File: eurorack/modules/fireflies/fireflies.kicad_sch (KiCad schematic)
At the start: 37 parts, among them J1 Conn_02x05_Odd_Even, U3 ProMicro

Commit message: fireflies schematic stuff
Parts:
- added J?: (no value), symbol Connector:AudioJack2_SwitchT
- added J? (x3): AudioJack2_SwitchT, symbol Connector:AudioJack2_SwitchT
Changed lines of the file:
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@@
     (pin "2")
+  )
+  (symbol (lib_id "Connector:AudioJack2_SwitchT") (at 181.864 77.978 0) (unit 1)
+    (in_bom yes) (on_board yes) (fields_autoplaced)
+    (property "Reference" "J?" (id 0) (at 181.229 68.58 0))
+    (property "Value" "" (id 1) (at 181.229 71.12 0))
+    (property "Footprint" "" (id 2) (at 181.864 77.978 0)
+      (effects (font (size 1.27 1.27)) hide)
+    )
+    (property "Datasheet" "~" (id 3) (at 181.864 77.978 0)
+      (effects (font (size 1.27 1.27)) hide)
+    )
+    (pin "S")
+    (pin "T")
+    (pin "TN")
   )
   (symbol (lib_id "Device:R") (at 87.122 174.752 90) (unit 1)
@@
     )
     (pin "1")
+  )
+  (symbol (lib_id "Connector:AudioJack2_SwitchT") (at 180.594 100.584 0) (unit 1)
+    (in_bom yes) (on_board yes) (fields_autoplaced)
+    (property "Reference" "J?" (id 0) (at 179.959 91.186 0))
+    (property "Value" "AudioJack2_SwitchT" (id 1) (at 179.959 93.726 0))
+    (property "Footprint" "" (id 2) (at 180.594 100.584 0)
+      (effects (font (size 1.27 1.27)) hide)
+    )
+    (property "Datasheet" "~" (id 3) (at 180.594 100.584 0)
+      (effects (font (size 1.27 1.27)) hide)
+    )
+    (pin "S")
+    (pin "T")
+    (pin "TN")
   )
   (symbol (lib_id "power:GND") (at 83.312 184.912 0) (unit 1)
@@
     (pin "1")
   )
+  (symbol (lib_id "Connector:AudioJack2_SwitchT") (at 209.042 99.06 0) (unit 1)
+    (in_bom yes) (on_board yes) (fields_autoplaced)
+    (property "Reference" "J?" (id 0) (at 208.407 89.662 0))
+    (property "Value" "AudioJack2_SwitchT" (id 1) (at 208.407 92.202 0))
+    (property "Footprint" "" (id 2) (at 209.042 99.06 0)
+      (effects (font (size 1.27 1.27)) hide)
+    )
+    (property "Datasheet" "~" (id 3) (at 209.042 99.06 0)
+      (effects (font (size 1.27 1.27)) hide)
+    )
+    (pin "S")
+    (pin "T")
+    (pin "TN")
+  )
   (symbol (lib_id "power:GND") (at 41.91 145.796 0) (unit 1)
     (in_bom yes) (on_board yes) (fields_autoplaced)
@@
     )
     (pin "1")
+  )
+  (symbol (lib_id "Connector:AudioJack2_SwitchT") (at 210.566 78.232 0) (unit 1)
+    (in_bom yes) (on_board yes) (fields_autoplaced)
+    (property "Reference" "J?" (id 0) (at 209.931 68.834 0))
+    (property "Value" "AudioJack2_SwitchT" (id 1) (at 209.931 71.374 0))
+    (property "Footprint" "" (id 2) (at 210.566 78.232 0)
+      (effects (font (size 1.27 1.27)) hide)
+    )
+    (property "Datasheet" "~" (id 3) (at 210.566 78.232 0)
+      (effects (font (size 1.27 1.27)) hide)
+    )
+    (pin "S")
+    (pin "T")
+    (pin "TN")
   )
   (symbol (lib_id "power:GND") (at 52.578 133.096 270) (unit 1)
@@
       (reference "J1") (unit 1) (value "Conn_02x05_Odd_Even") (footprint "Connector_PinHeader_2.54mm:PinHeader_2x05_P2.54mm_Vertical_SMD")
     )
+    (path "/7fec32f7-4e07-4832-9024-4f9fa14f8485"
+      (reference "J?") (unit 1) (value "AudioJack2_SwitchT") (footprint "")
+    )
+    (path "/9269573e-337a-438e-bed5-4bfb6f1dd25c"
+      (reference "J?") (unit 1) (value "AudioJack2_SwitchT") (footprint "")
+    )
+    (path "/e0d100f4-64a0-4b05-af9e-33a716f9f45b"
+      (reference "J?") (unit 1) (value "AudioJack2_SwitchT") (footprint "")
+    )
+    (path "/e653be94-887e-48f2-9e69-61973902ec02"
+      (reference "J?") (unit 1) (value "AudioJack2_SwitchT") (footprint "")
+    )
     (path "/a7cbf3ab-685a-48fb-b5f0-6b3e0a12818c"

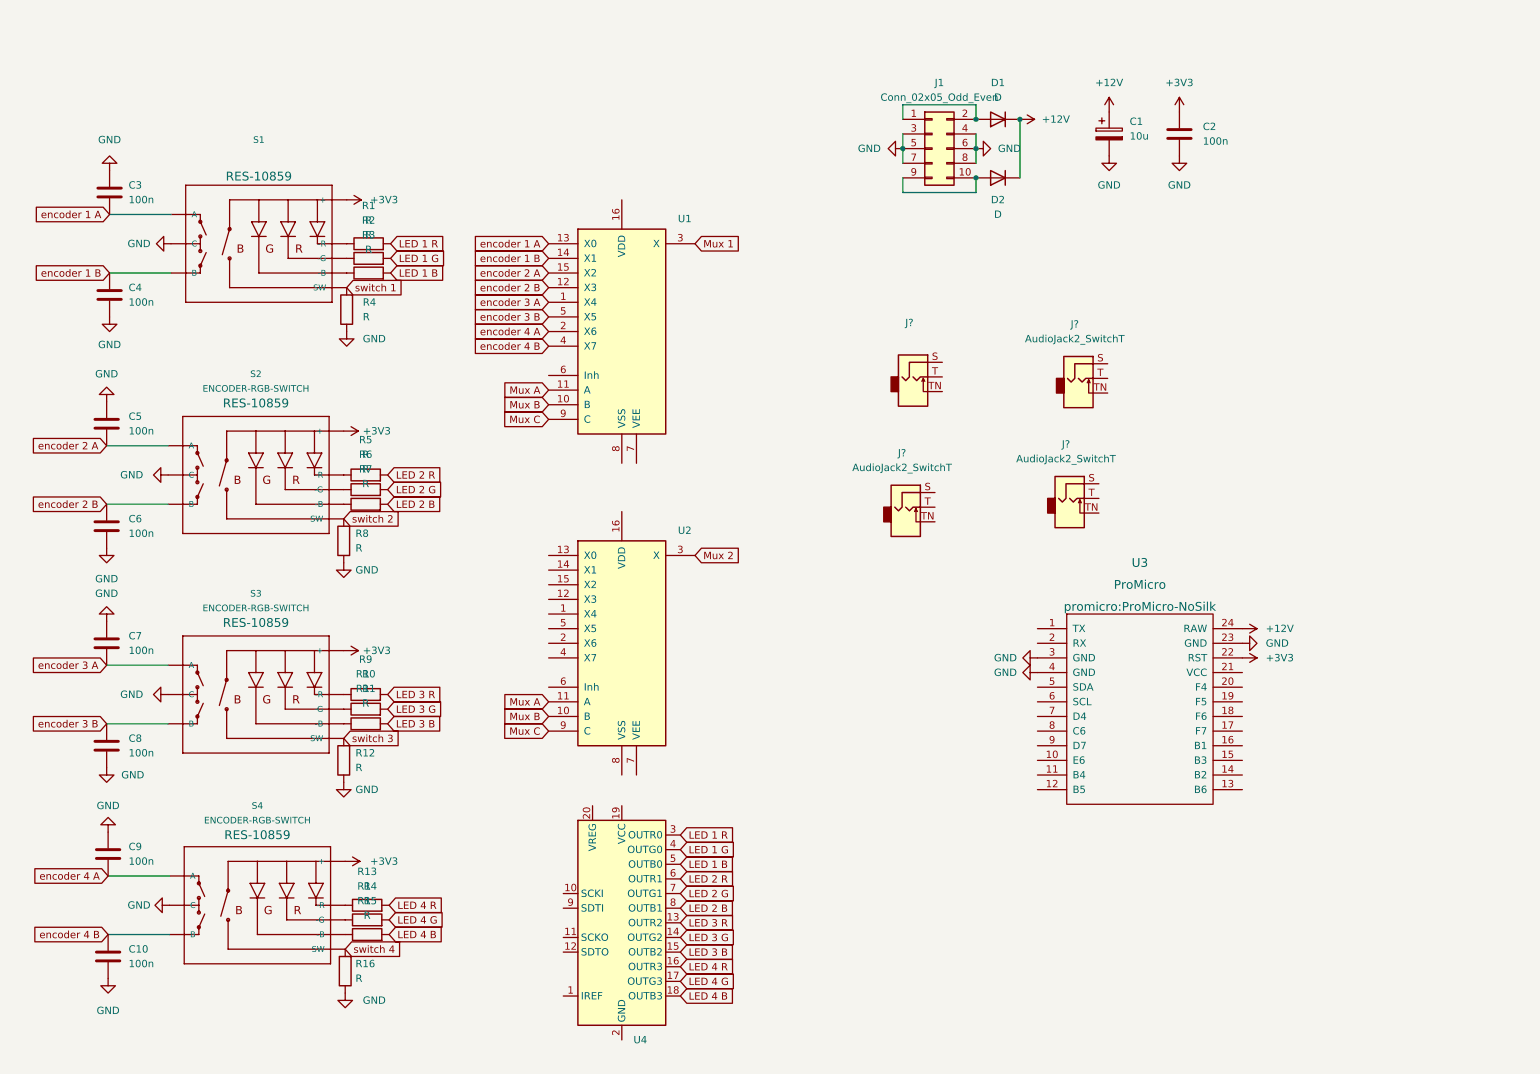
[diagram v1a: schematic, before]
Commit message: cicadas: normal clock input to 3v3 and fix missing ground connections
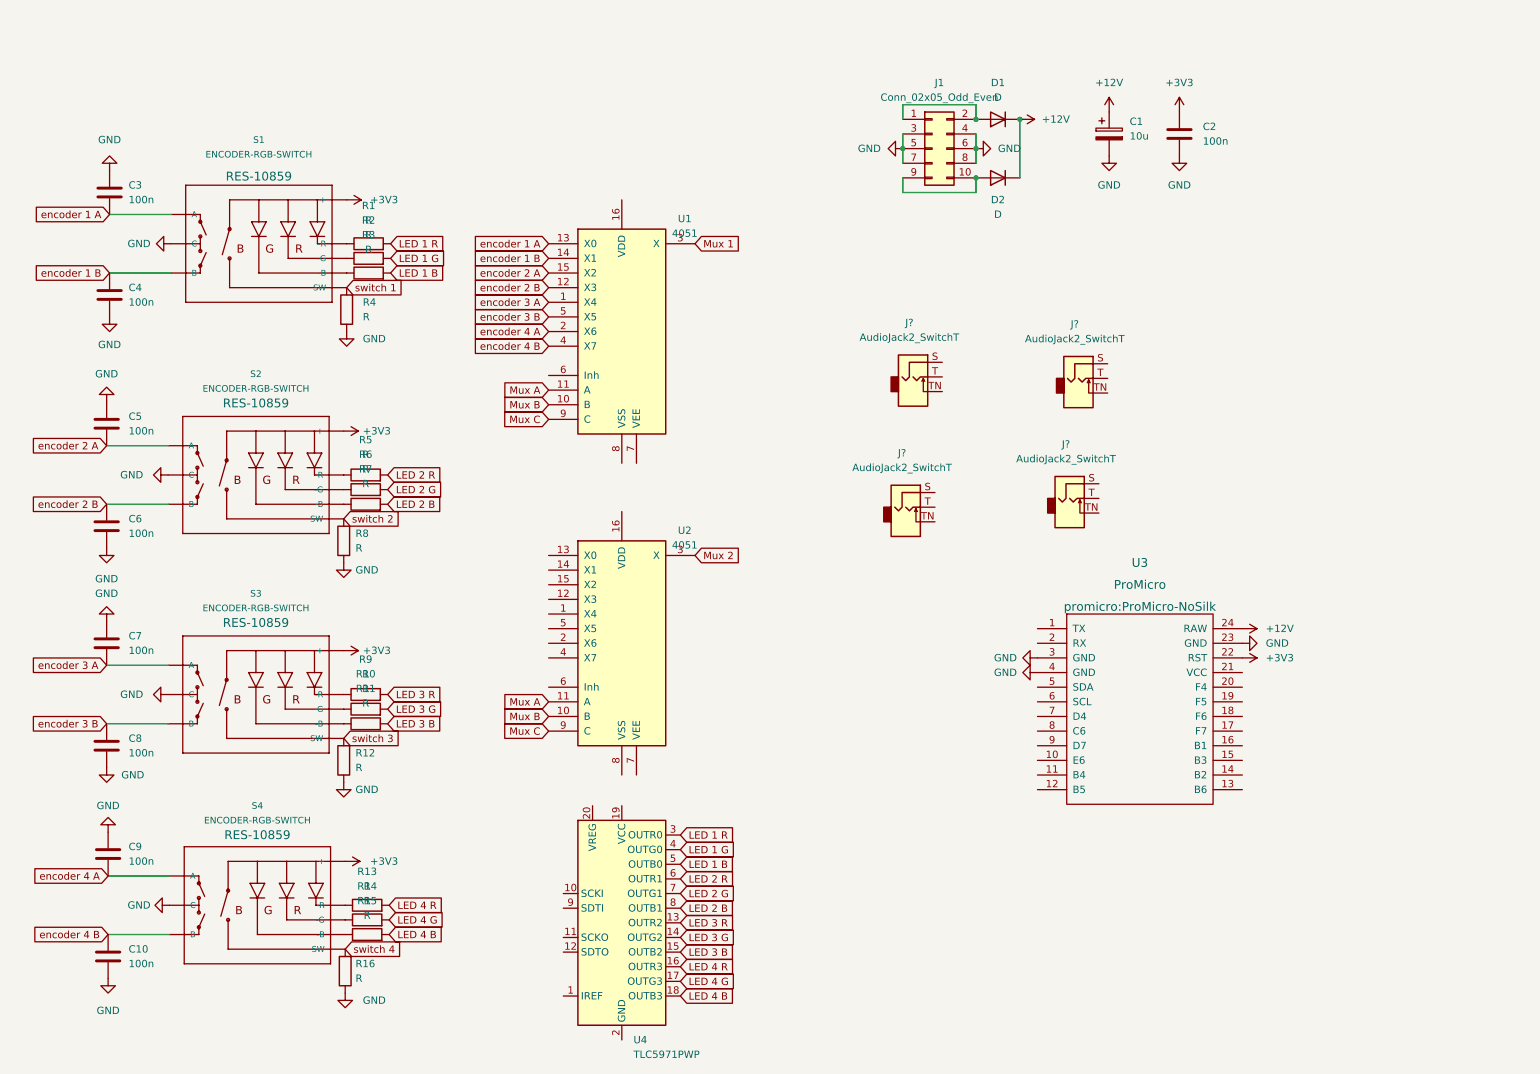
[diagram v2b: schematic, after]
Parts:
- J?: value (none) -> AudioJack2_SwitchT
- S1: value (none) -> ENCODER-RGB-SWITCH; footprint (none) -> Switches:ENCODER_LED_3
- U1, U2: value (none) -> 4051; footprint (none) -> Package_SO:TSSOP-16_4.4x5mm_P0.65mm
- U4: value (none) -> TLC5971PWP; footprint (none) -> Package_SO:HTSSOP-20-1EP_4.4x6.5mm_P0.65mm_EP3.4x6.5mm_Mask2.75x3.43mm_ThermalVias
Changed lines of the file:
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@@
       (effects (font (size 1.143 1.143)))
     )
-    (property "Value" "" (id 1) (at 68.326 39.37 0)
+    (property "Value" "ENCODER-RGB-SWITCH" (id 1) (at 68.326 39.37 0)
       (effects (font (size 1.143 1.143)))
     )
-    (property "Footprint" "" (id 2) (at 68.326 40.894 0)
+    (property "Footprint" "Switches:ENCODER_LED_3" (id 2) (at 68.326 40.894 0)
       (effects (font (size 0.508 0.508)) hide)
     )
@@
     (in_bom yes) (on_board yes) (fields_autoplaced)
     (property "Reference" "U2" (id 0) (at 142.24 104.6353 0))
-    (property "Value" "" (id 1) (at 142.24 107.1753 0))
-    (property "Footprint" "" (id 2) (at 131.318 124.206 0)
+    (property "Value" "4051" (id 1) (at 142.24 107.1753 0))
+    (property "Footprint" "Package_SO:TSSOP-16_4.4x5mm_P0.65mm" (id 2) (at 131.318 124.206 0)
       (effects (font (size 1.27 1.27)) hide)
     )
@@
     (in_bom yes) (on_board yes) (fields_autoplaced)
     (property "Reference" "U1" (id 0) (at 142.24 50.5333 0))
-    (property "Value" "" (id 1) (at 142.24 53.0733 0))
-    (property "Footprint" "" (id 2) (at 131.318 70.104 0)
+    (property "Value" "4051" (id 1) (at 142.24 53.0733 0))
+    (property "Footprint" "Package_SO:TSSOP-16_4.4x5mm_P0.65mm" (id 2) (at 131.318 70.104 0)
       (effects (font (size 1.27 1.27)) hide)
     )
@@
     (in_bom yes) (on_board yes) (fields_autoplaced)
     (property "Reference" "J?" (id 0) (at 181.229 68.58 0))
-    (property "Value" "" (id 1) (at 181.229 71.12 0))
+    (property "Value" "AudioJack2_SwitchT" (id 1) (at 181.229 71.12 0))
     (property "Footprint" "" (id 2) (at 181.864 77.978 0)
       (effects (font (size 1.27 1.27)) hide)
@@
       (effects (font (size 1.27 1.27)) (justify left))
     )
-    (property "Value" "" (id 1) (at 133.3374 195.58 0)
-      (effects (font (size 1.27 1.27)) (justify left))
-    )
-    (property "Footprint" "" (id 2) (at 132.588 194.31 0)
+    (property "Value" "TLC5971PWP" (id 1) (at 133.3374 195.58 0)
+      (effects (font (size 1.27 1.27)) (justify left))
+    )
+    (property "Footprint" "Package_SO:HTSSOP-20-1EP_4.4x6.5mm_P0.65mm_EP3.4x6.5mm_Mask2.75x3.43mm_ThermalVias" (id 2) (at 132.588 194.31 0)
       (effects (font (size 1.27 1.27)) (justify left) hide)
     )

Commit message: start rethinking fireflies around chordata
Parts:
- removed C1: 10u, Capacitor_SMD:CP_Elec_5x4.5, symbol Device:C_Polarized
- removed C2: 100n, Capacitor_SMD:C_0805_2012Metric_Pad1.18x1.45mm_HandSolder, symbol Device:C
- removed D1, D2: D, Diode_SMD:D_SOD-123, symbol Device:D
- removed J1: Conn_02x05_Odd_Even, Connector_PinHeader_2.54mm:PinHeader_2x05_P2.54mm_Vertical_SMD, symbol Connector_Generic:Conn_02x05_Odd_Even
- removed R13, R14, R6: R, Resistor_SMD:R_0805_2012Metric_Pad1.20x1.40mm_HandSolder, symbol Device:R
- removed U1, U2: 4051, Package_SO:TSSOP-16_4.4x5mm_P0.65mm, symbol 4xxx:4051
- removed U3: ProMicro, promicro:ProMicro-NoSilk, symbol promicro:ProMicro
- added C10, C7: 100n, Capacitor_SMD:C_0805_2012Metric_Pad1.18x1.45mm_HandSolder, symbol Device:C
- added C12: 1u, Capacitor_SMD:C_0805_2012Metric_Pad1.18x1.45mm_HandSolder, symbol Device:C
- added C4, C5: 10u, Capacitor_SMD:C_0805_2012Metric_Pad1.18x1.45mm_HandSolder, symbol Device:C
- added D1, D2: D_Zener, Diode_SMD:D_0805_2012Metric_Pad1.15x1.40mm_HandSolder, symbol Device:D_Zener
- added J1: (no value), symbol Connector_Generic:Conn_01x04
- added R4: 10k, Resistor_SMD:R_0805_2012Metric_Pad1.20x1.40mm_HandSolder, symbol Device:R
- added R8: (no value), Resistor_SMD:R_0805_2012Metric_Pad1.20x1.40mm_HandSolder, symbol Device:R
- added SW1, SW2: SW_Push_LED, Pale Slim Ghost:PB01-109TL, symbol Switch:SW_Push_LED
- added U1: MIC5219-5.0YM5, Package_TO_SOT_SMD:SOT-23-5, symbol Regulator_Linear:MIC5219-5.0YM5
- added U2: Chordata, Pale Slim Ghost:Chordata, symbol Pale Slim Ghost:Chordata
- added U3: MCP4822, Package_SO:MSOP-8_3x3mm_P0.65mm, symbol Analog_DAC:MCP4822
- J2, J3, J4, J5: renamed from J?; footprint (none) -> Pale Slim Ghost:Jack_3.5mm_QingPu_WQP-PJ398SM_Vertical
- R1, R15, R7: value R -> 4k7
- R10, R2: value R -> 1k
- R11, R5: value R -> 560
- R12: renamed from R8; value R -> (none)
- R13: renamed from R12; value R -> (none)
- R14: renamed from R16; value R -> (none)
- R3: value R -> 10k
- R6: renamed from R4; value R -> (none)
- R9: value R -> (none)
- S1, S2, S3, S4: footprint Switches:ENCODER_LED_3 -> Pale Slim Ghost:ENCODER_LED_3
- renumbered C3 to C1, C9 to C11, C10 to C13, C4 to C2, C5 to C3, C7 to C8, C8 to C9
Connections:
- net +12V: now also U4.19 (VCC), C10.2, C4.1, U1.1 (IN), U1.3 (EN), U2.17 (+12V)
- net +3V3: now also SW1.1, SW2.1, U2.36 (+3V3)
- net GND: now also J2.S, J3.S, J4.S, J5.S, R1.2, R15.1, R7.2, U4.2 (GND), U4.21 (GND), C10.1, C12.2, C4.2, C5.2, C7.1, D1.2 (A), D2.2 (A), J1.4 (Pin_4), SW1.L2 (K), SW2.L2 (K), U1.2 (GND), U2.18 (GND), U2.19 (GND), U2.35 (GND), U3.7 (Vss)
- net LED 1 B: now also S1.4 (-B); no longer R3.2
- net LED 1 G: now also S1.2 (-G); no longer R2.2
- net LED 1 R: now also S1.1 (-R); no longer R1.2
- net LED 2 B: now also S2.4 (-B); no longer R7.2
- net LED 2 G: now also S2.2 (-G)
- net LED 2 R: now also S2.1 (-R); no longer R5.2
- net LED 3 B: now also S3.4 (-B); no longer R11.2
- net LED 3 G: now also S3.2 (-G); no longer R10.2
- net LED 3 R: now also S3.1 (-R); no longer R9.2
- net LED 4 B: now also S4.4 (-B); no longer R15.2
- net LED 4 G: now also S4.2 (-G)
- net LED 4 R: now also S4.1 (-R)
- net encoder 1 A: now also U2.1 (GPIO0)
- net encoder 1 B: now also U2.31 (GPIO26_ADC0)
- net encoder 2 A: now also U2.3 (GPIO2)
- net encoder 2 B: now also U2.30 (GPIO25)
- net encoder 3 A: now also U2.29 (GPIO24)
- net encoder 3 B: now also U2.4 (GPIO3)
- net encoder 4 A: now also U2.28 (GPIO23)
- net encoder 4 B: now also U2.6 (GPIO5)
- net at R9.1: now also J5.T; no longer S3.1 (-R)
- net Switch 2: now reaches R10.1
- net Switch 2: now also U2.11 (GPIO10); no longer S3.2 (-G)
- net at R11.1: now also SW2.L1 (A); no longer S3.4 (-B)
- net at R1.1: now also R2.2, SW1.2; no longer S1.1 (-R)
- net Switch 1: now reaches R2.1
- net Switch 1: now also U2.9 (GPIO8); no longer S1.2 (-G)
- net at R3.1: now also J2.T; no longer S1.4 (-B)
- net at R7.1: now also R10.2, SW2.2; no longer S2.4 (-B)
- net at R5.1: now also SW1.L1 (A); no longer S2.1 (-R)
- net at J4.T: now also R8.1
- net at U4.1 (IREF): now also R15.2
- net SCK2: now reaches U4.10 (SCKI)
- net SCK2: now also U2.15 (GPIO14)
- net at U4.20 (VREG): now also C12.1
- net COPI2: now reaches U4.9 (SDTI)
- net COPI2: now also U2.16 (GPIO15)
- net at J3.T: now also R4.1
- net switch 1 renamed encoder 1 switch
- net encoder 1 switch: now also U2.34 (GPIO29_ADC3)
- net switch 2 renamed encoder 2 switch
- net encoder 2 switch: now also U2.2 (GPIO1)
- net switch 3 renamed encoder 3 switch
- net encoder 3 switch: now also U2.5 (GPIO4)
- net switch 4 renamed encoder 4 switch
- net encoder 4 switch: now also U2.7 (GPIO6)
- new net +5V: C5.1, C7.2, U1.5 (OUT), U3.1 (Vdd)
- new net -12V: U2.20 (-12V)
- new net COPI1: U2.24 (GPIO19), U3.4 (SDI)
- new net CS1: U2.21 (GPIO16), U3.2 (~{CS})
- new net Input 1: D1.1 (K), R3.2, U2.33 (GPIO28_ADC2)
- new net Input 2: D2.1 (K), R4.2, U2.32 (GPIO27_ADC1)
- new net Output 1: R8.2, U3.8 (VA)
- new net Output 2: R9.2, U3.6 (VB)
- new net SCK1: U2.23 (GPIO18), U3.3 (SCK)
- new net SCL: J1.1 (Pin_1), U2.26 (GPIO21)
- new net SDA: J1.2 (Pin_2), U2.25 (GPIO20)
- new net Switch LED 1: R5.2, U2.10 (GPIO9)
- new net Switch LED 2: R11.2, U2.12 (GPIO11)
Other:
- moved on the sheet: C1, C11, C13, C2, C3, C6, C8, C9, J2, J3, J4, J5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
